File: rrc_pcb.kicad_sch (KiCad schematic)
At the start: 13 parts, among them J1 Voltage Regulator Input, J2 Conn_01x03_Male, U1 ADXL357Z, U2 Teensy3.6-teensy, U3 BN220-GPS, U4 MS5611, U5 logo

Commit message: updated .sch
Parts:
- removed RF11: RFD900+-RF_Module, rfd900+:RFD900+, symbol parts:RFD900+-RF_Module
- removed U1: ADXL357Z, adxl357z:ADXL357, symbol parts:ADXL357Z
- added U1: iridium9602, symbol parts:iridium9602
- added U6: ICM-20948, QFN40P300X300X105-24N, symbol parts:ICM-20948
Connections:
- net +5V: now also U1.1 (5V)
- net GND: now also U1.4 (GND)
- net T_GND: now also U6.18 (GND), U6.19 (RESV_19), U6.20 (RESV_20)
- net T_VCC: now also U6.13 (VDD), U6.8 (VDDIO)
- net RX2: now reaches U2.11 (9_PWM_RX2_CS0)
- net RX2: now also U1.3 (TX)
- net TX2: now reaches U2.12 (10_PWM_TX2_CS0)
- net TX2: now also U1.2 (RX)
- net at U2.45 (18_A4_SDA0_TOUCH): no longer R2.1
- net at U2.46 (19_A5_SCL0_TOUCH): no longer R1.1
- net at U2.~ (GND): now also R2.1, U6.24 (SDA/SDI)
- new net: R1.1, U2.~ (GND), U6.23 (SCL/SCLK)
- new net: U6.1 (NC), U6.14 (NC), U6.15 (NC), U6.16 (NC), U6.17 (NC), U6.2 (NC), U6.3 (NC), U6.4 (NC), U6.5 (NC), U6.6 (NC)
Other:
- moved on the sheet: J1, J2, R1, R2

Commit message: update 2
updated .sch added teensy4.1 , and updated footprints. Still in debugging stage
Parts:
- removed U2: Teensy3.6-teensy, teensy:Teensy35_36, symbol parts:Teensy3.6-teensy
- added U2: DEV-16771, teensy:Teensy41, symbol parts:DEV-16771
- U1: footprint (none) -> Connector_PinHeader_2.54mm:PinHeader_1x04_P2.54mm_Horizontal
- U4: renamed from U6; footprint QFN40P300X300X105-24N -> Connector_PinHeader_2.54mm:PinHeader_2x10_P2.54mm_Vertical
- renumbered U4 to U5, U5 to U6
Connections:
- net +5V: now also U2.VIN; no longer U1.1 (5V)
- net GND: now also U2.GND1 (GND), U2.GND2 (GND), U2.GND3 (GND), U2.GND4 (GND), U2.GND5 (GND)
- net RX2: now also U2.7 (RX2)
- net TX2: now also U2.8 (TX2)
- net T_GND: now also U2.USB_GND1 (USB_GND), U2.USB_GND2 (USB_GND)
- net T_VCC: now also U1.1 (5V), U2.5V
- net RX1: now reaches U3.3 (TX)
- net RX1: now also U2.0 (RX1)
- net at J2.2 (Pin_2): now also U2.23 (A9)
- net at BZ1.1 (-): now also U2.41 (A17)
- net TX1: now reaches U3.2 (RX)
- net TX1: now also U2.1 (TX1)
- net SCL1: now reaches R3.1, U5.3 (SCL)
- net SCL1: now also U2.16 (A2)
- net SDA1: now reaches R4.1, U5.4 (SDA)
- net SDA1: now also U2.17 (A3)
- net at R1.1, U4.23 (SCL/SCLK): now also U2.19 (A5)
- net at R2.1, U4.24 (SDA/SDI): now also U2.18 (A4)
- new net: U2.3.3V_1 (3.3V), U2.3.3V_2 (3.3V), U2.3.3V_3 (3.3V)
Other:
- moved on the sheet: BZ1, J1, J2, R1, R2, R3, R4, U1, U3, U4, U5, U6

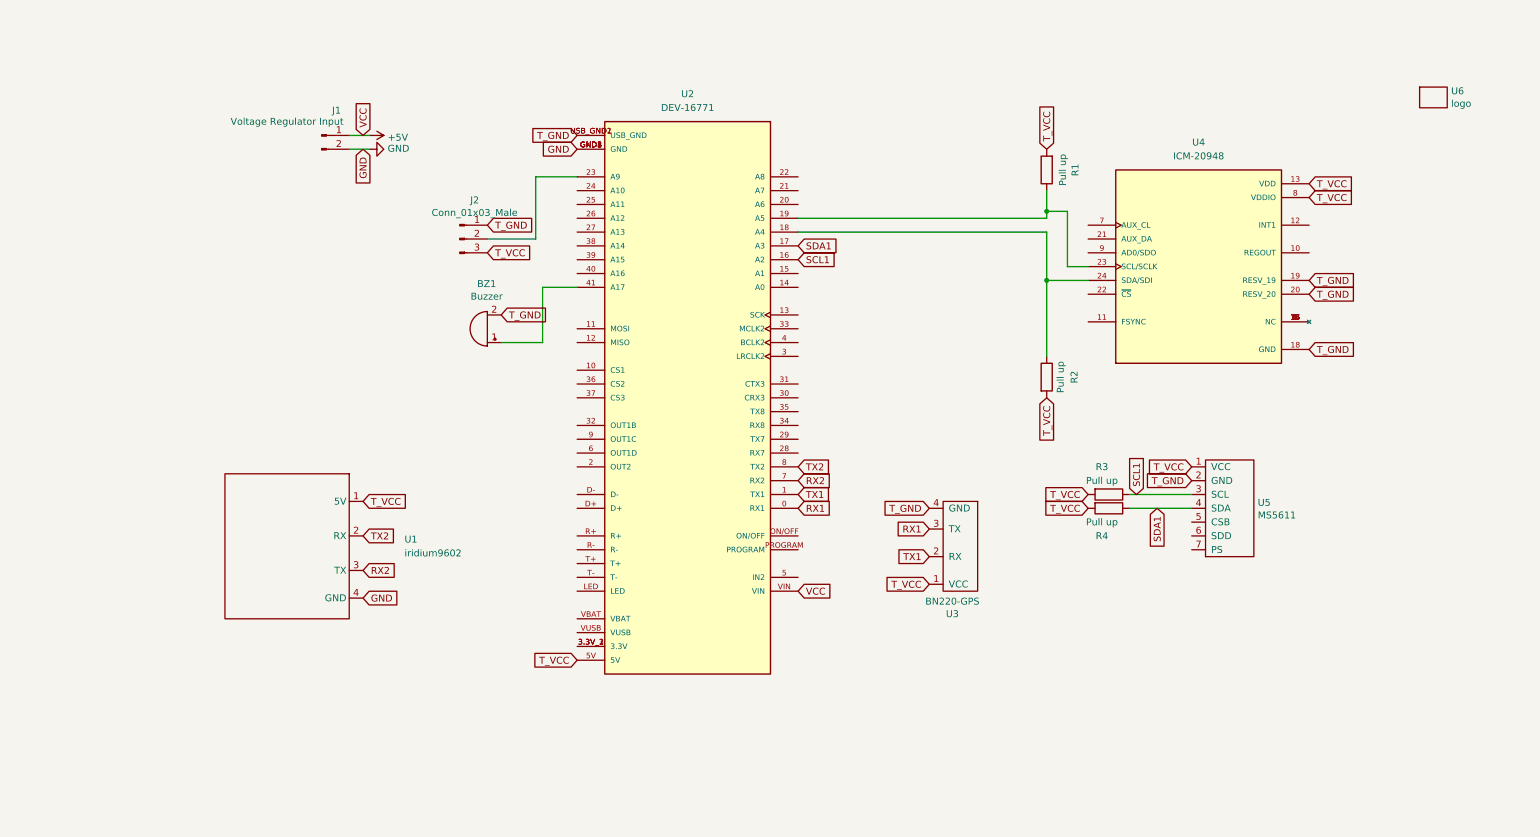
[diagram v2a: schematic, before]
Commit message: updated pcb footprints
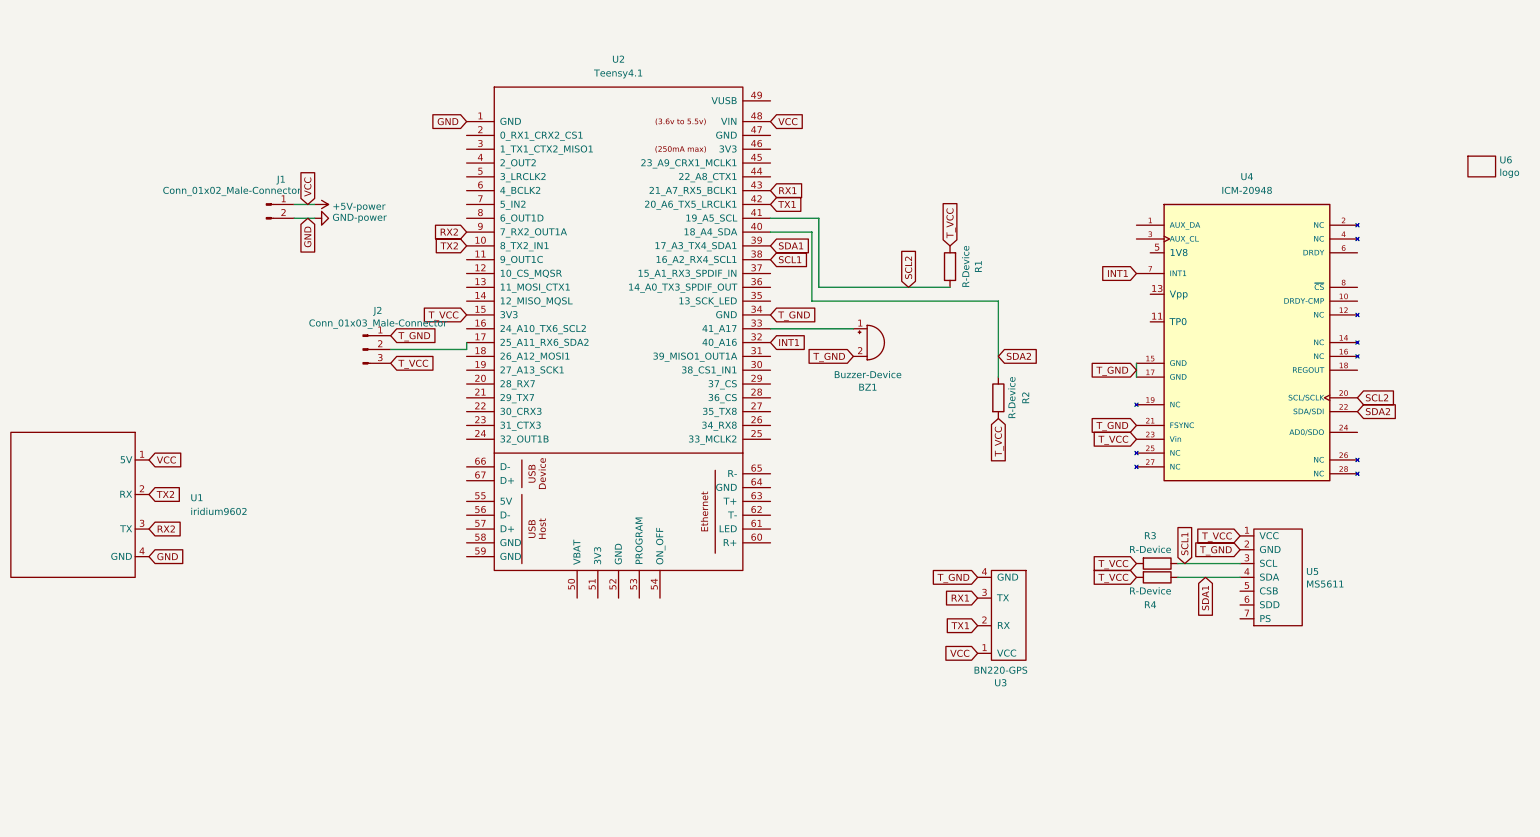
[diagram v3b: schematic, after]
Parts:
- removed U2: DEV-16771, teensy:Teensy41, symbol parts:DEV-16771
- removed U4: ICM-20948, Connector_PinHeader_2.54mm:PinHeader_2x10_P2.54mm_Vertical, symbol parts:ICM-20948
- added U2: Teensy4.1, teensy:Teensy41, symbol teensy:Teensy4.1
- added U4: ICM-20948, Connector_PinHeader_2.54mm:PinHeader_2x14_P2.54mm_Vertical, symbol parts:ICM-20948
- BZ1: value Buzzer -> Buzzer-Device
- J1: value Voltage Regulator Input -> Conn_01x02_Male-Connector
- J2: value Conn_01x03_Male -> Conn_01x03_Male-Connector
- R1, R2, R3, R4: value Pull up -> R-Device
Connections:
- net +5V: now also U1.1 (5V), U3.1 (VCC), U2.48 (VIN)
- net GND: now also U2.1 (GND)
- net RX1: now also U2.43 (21_A7_RX5_BCLK1)
- net RX2: now also U2.9 (7_RX2_OUT1A)
- net SCL1: now also U2.38 (16_A2_RX4_SCL1)
- net SDA1: now also U2.39 (17_A3_TX4_SDA1)
- net TX1: now also U2.42 (20_A6_TX5_LRCLK1)
- net TX2: now also U2.10 (8_TX2_IN1)
- net T_GND: now also U2.34 (GND), U4.15 (GND), U4.17 (GND), U4.21 (FSYNC)
- net T_VCC: now also U2.15 (3V3), U4.23 (Vin); no longer U1.1 (5V), U3.1 (VCC)
- net SCL2: now reaches R1.1
- net SCL2: now also U2.41 (19_A5_SCL), U4.20 (SCL/SCLK)
- net SDA2: now reaches R2.1
- net SDA2: now also U2.40 (18_A4_SDA), U4.22 (SDA/SDI)
- net at BZ1.1 (-): now also U2.33 (41_A17)
- net at J2.2 (Pin_2): now also U2.17 (25_A11_RX6_SDA2)
- new net INT1: U2.32 (40_A16), U4.7 (INT1)
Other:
- moved on the sheet: BZ1, J1, J2, R1, R2, R3, R4, U1, U3, U5, U6

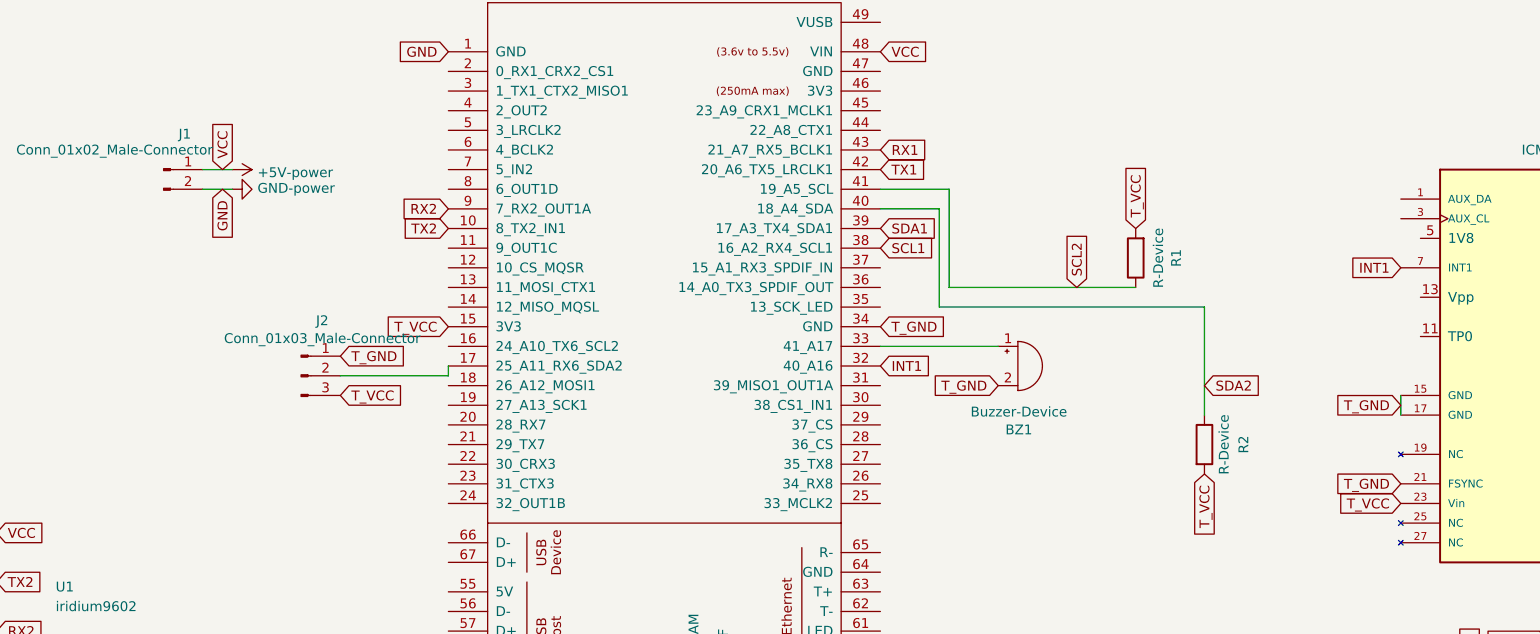
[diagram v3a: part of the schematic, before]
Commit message: optimized and finalized pcb
reduced sizing and fixed traces.
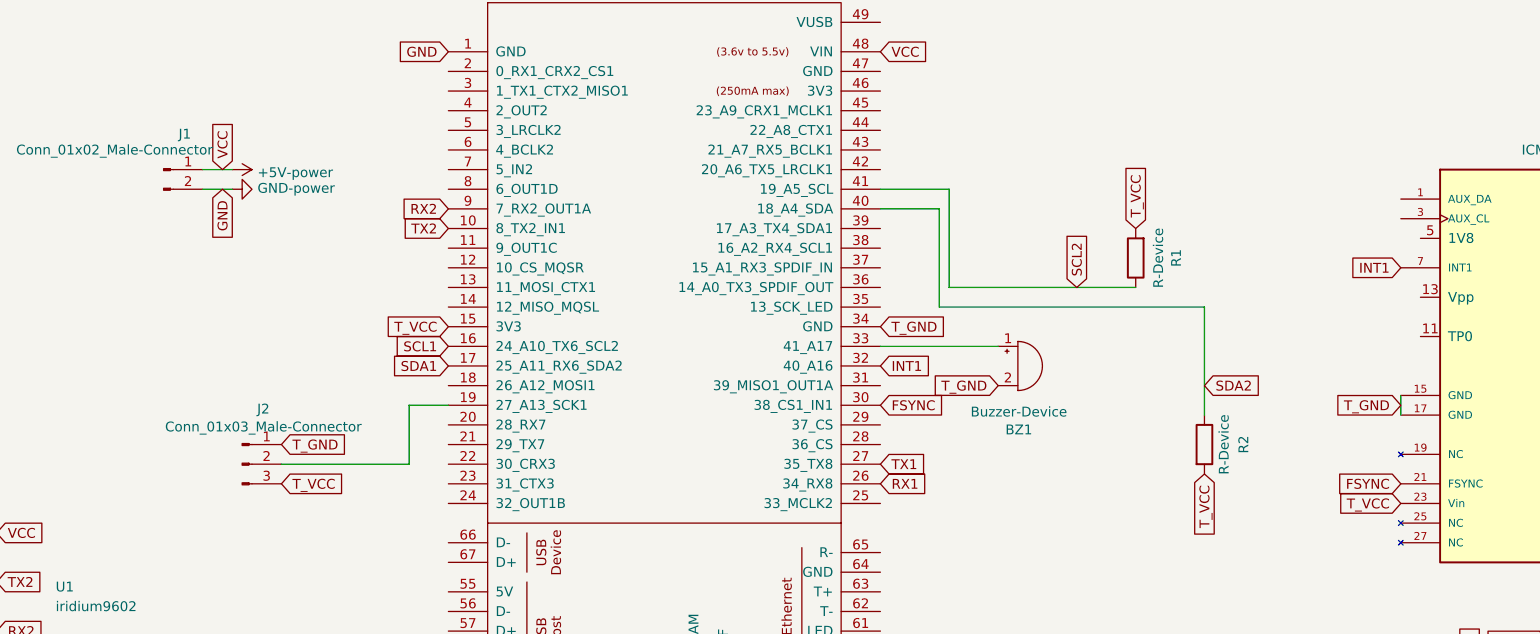
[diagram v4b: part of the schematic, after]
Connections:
- net RX1: now also U2.26 (34_RX8); no longer U2.43 (21_A7_RX5_BCLK1)
- net SCL1: now also U2.16 (24_A10_TX6_SCL2); no longer U2.38 (16_A2_RX4_SCL1)
- net SDA1: now also U2.17 (25_A11_RX6_SDA2); no longer U2.39 (17_A3_TX4_SDA1)
- net TX1: now also U2.27 (35_TX8); no longer U2.42 (20_A6_TX5_LRCLK1)
- net T_GND: no longer U4.21 (FSYNC)
- net at J2.2 (Pin_2): now also U2.19 (27_A13_SCK1); no longer U2.17 (25_A11_RX6_SDA2)
- net FSYNC: now reaches U2.30 (38_CS1_IN1)
- net FSYNC: now also U4.21 (FSYNC)
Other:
- moved on the sheet: J2
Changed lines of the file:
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@@
-    (stroke (width 0) (type default) (color 0 0 0 0))
-  )
-  (wire (pts (xy 85.09 63.5) (xy 99.06 63.5))
     (stroke (width 0) (type default) (color 0 0 0 0))
   )
@@
     (stroke (width 0) (type default) (color 0 0 0 0))
   )
+  (wire (pts (xy 77.47 74.93) (xy 93.98 74.93))
+    (stroke (width 0) (type default) (color 0 0 0 0))
+  )
   (wire (pts (xy 163.83 52.07) (xy 187.96 52.07))
     (stroke (width 0) (type default) (color 0 0 0 0))
@@
     (stroke (width 0) (type default) (color 0 0 0 0))
   )
+  (wire (pts (xy 93.98 67.31) (xy 99.06 67.31))
+    (stroke (width 0) (type default) (color 0 0 0 0))
+  )
+  (wire (pts (xy 93.98 74.93) (xy 93.98 67.31))
+    (stroke (width 0) (type default) (color 0 0 0 0))
+  )
   (wire (pts (xy 163.83 52.07) (xy 163.83 39.37))
     (stroke (width 0) (type default) (color 0 0 0 0))
@@
     (stroke (width 0) (type default) (color 0 0 0 0))
   )
-  (wire (pts (xy 99.06 63.5) (xy 99.06 62.23))
-    (stroke (width 0) (type default) (color 0 0 0 0))
-  )
   (wire (pts (xy 162.56 54.61) (xy 162.56 41.91))
     (stroke (width 0) (type default) (color 0 0 0 0))
   )
+  (global_label "FSYNC" (shape input) (at 222.25 77.47 180) (fields_autoplaced)
+    (effects (font (size 1.27 1.27)) (justify right))
+    (property "Intersheet References" "${INTERSHEET_REFS}" (id 0) (at 213.9387 77.3906 0)
+      (effects (font (size 1.27 1.27)) (justify right) hide)
+    )
+  )
   (global_label "T_GND" (shape input) (at 222.25 67.31 180) (fields_autoplaced)
     (effects (font (size 1.27 1.27)) (justify right))
@@
     )
   )
-  (global_label "TX1" (shape input) (at 154.94 36.83 0) (fields_autoplaced)
-    (effects (font (size 1.27 1.27)) (justify left))
-    (property "Intersheet References" "${INTERSHEET_REFS}" (id 0) (at 160.6509 36.7506 0)
-      (effects (font (size 1.27 1.27)) (justify left) hide)
-    )
-  )
-  (global_label "SDA1" (shape input) (at 154.94 44.45 0) (fields_autoplaced)
-    (effects (font (size 1.27 1.27)) (justify left))
-    (property "Intersheet References" "${INTERSHEET_REFS}" (id 0) (at 162.0418 44.3706 0)
-      (effects (font (size 1.27 1.27)) (justify left) hide)
-    )
-  )
-  (global_label "T_GND" (shape input) (at 85.09 60.96 0) (fields_autoplaced)
-    (effects (font (size 1.27 1.27)) (justify left))
-    (property "Intersheet References" "${INTERSHEET_REFS}" (id 0) (at 20.32 -59.69 0)
+  (global_label "T_GND" (shape input) (at 77.47 72.39 0) (fields_autoplaced)
+    (effects (font (size 1.27 1.27)) (justify left))
+    (property "Intersheet References" "${INTERSHEET_REFS}" (id 0) (at 12.7 -48.26 0)
       (effects (font (size 1.27 1.27)) hide)
     )
@@
     )
   )
-  (global_label "T_VCC" (shape input) (at 85.09 66.04 0) (fields_autoplaced)
-    (effects (font (size 1.27 1.27)) (justify left))
-    (property "Intersheet References" "${INTERSHEET_REFS}" (id 0) (at 20.32 -59.69 0)
-      (effects (font (size 1.27 1.27)) hide)
-    )
-  )
-  (global_label "RX1" (shape input) (at 154.94 34.29 0) (fields_autoplaced)
-    (effects (font (size 1.27 1.27)) (justify left))
-    (property "Intersheet References" "${INTERSHEET_REFS}" (id 0) (at 160.9532 34.2106 0)
+  (global_label "RX1" (shape input) (at 154.94 77.47 0) (fields_autoplaced)
+    (effects (font (size 1.27 1.27)) (justify left))
+    (property "Intersheet References" "${INTERSHEET_REFS}" (id 0) (at 160.9532 77.3906 0)
+      (effects (font (size 1.27 1.27)) (justify left) hide)
+    )
+  )
+  (global_label "T_VCC" (shape input) (at 77.47 77.47 0) (fields_autoplaced)
+    (effects (font (size 1.27 1.27)) (justify left))
+    (property "Intersheet References" "${INTERSHEET_REFS}" (id 0) (at 12.7 -48.26 0)
+      (effects (font (size 1.27 1.27)) hide)
+    )
+  )
+  (global_label "FSYNC" (shape input) (at 154.94 67.31 0) (fields_autoplaced)
+    (effects (font (size 1.27 1.27)) (justify left))
+    (property "Intersheet References" "${INTERSHEET_REFS}" (id 0) (at 163.2513 67.2306 0)
       (effects (font (size 1.27 1.27)) (justify left) hide)
     )
@@
     )
   )
+  (global_label "SCL1" (shape input) (at 99.06 59.69 180) (fields_autoplaced)
+    (effects (font (size 1.27 1.27)) (justify right))
+    (property "Intersheet References" "${INTERSHEET_REFS}" (id 0) (at 92.0187 59.6106 0)
+      (effects (font (size 1.27 1.27)) (justify right) hide)
+    )
+  )
   (global_label "T_VCC" (shape input) (at 222.25 80.01 180) (fields_autoplaced)
     (effects (font (size 1.27 1.27)) (justify right))
@@
     )
   )
+  (global_label "SDA1" (shape input) (at 99.06 62.23 180) (fields_autoplaced)
+    (effects (font (size 1.27 1.27)) (justify right))
+    (property "Intersheet References" "${INTERSHEET_REFS}" (id 0) (at 91.9582 62.3094 0)
+      (effects (font (size 1.27 1.27)) (justify right) hide)
+    )
+  )
   (global_label "INT1" (shape input) (at 222.25 49.53 180) (fields_autoplaced)
     (effects (font (size 1.27 1.27)) (justify right))
@@
     )
   )
-  (global_label "T_GND" (shape input) (at 222.25 77.47 180) (fields_autoplaced)
-    (effects (font (size 1.27 1.27)) (justify right))
-    (property "Intersheet References" "${INTERSHEET_REFS}" (id 0) (at 361.95 -162.56 0)
-      (effects (font (size 1.27 1.27)) hide)
-    )
-  )
   (global_label "T_GND" (shape input) (at 241.3 100.33 180) (fields_autoplaced)
     (effects (font (size 1.27 1.27)) (justify right))
@@
     )
   )
-  (global_label "SCL1" (shape input) (at 154.94 46.99 0) (fields_autoplaced)
-    (effects (font (size 1.27 1.27)) (justify left))
-    (property "Intersheet References" "${INTERSHEET_REFS}" (id 0) (at 161.9813 47.0694 0)
-      (effects (font (size 1.27 1.27)) (justify left) hide)
-    )
-  )
   (global_label "T_GND" (shape input) (at 154.94 57.15 0) (fields_autoplaced)
     (effects (font (size 1.27 1.27)) (justify left))
@@
     (effects (font (size 1.27 1.27)) (justify left))
     (property "Intersheet References" "${INTERSHEET_REFS}" (id 0) (at 269.9313 72.3106 0)
+      (effects (font (size 1.27 1.27)) (justify left) hide)
+    )
+  )
+  (global_label "TX1" (shape input) (at 154.94 74.93 0) (fields_autoplaced)
+    (effects (font (size 1.27 1.27)) (justify left))
+    (property "Intersheet References" "${INTERSHEET_REFS}" (id 0) (at 160.6509 74.8506 0)
       (effects (font (size 1.27 1.27)) (justify left) hide)
     )
@@
     )
   )
-  (symbol (lib_id "rrc_pcb-rescue:Conn_01x03_Male-Connector") (at 80.01 63.5 0) (unit 1)
-    (in_bom yes) (on_board yes)
-    (property "Reference" "J2" (id 0) (at 82.7532 56.3626 0))
-    (property "Value" "Conn_01x03_Male-Connector" (id 1) (at 82.7532 58.674 0))
-    (property "Footprint" "Connector_PinHeader_2.54mm:PinHeader_1x03_P2.54mm_Vertical" (id 2) (at 80.01 63.5 0)
-      (effects (font (size 1.27 1.27)) hide)
-    )
-    (property "Datasheet" "~" (id 3) (at 80.01 63.5 0)
-      (effects (font (size 1.27 1.27)) hide)
-    )
+  (symbol (lib_id "rrc_pcb-rescue:Conn_01x03_Male-Connector") (at 72.39 74.93 0) (unit 1)
+    (in_bom yes) (on_board yes)
+    (property "Reference" "J2" (id 0) (at 75.1332 67.7926 0))
+    (property "Value" "Conn_01x03_Male-Connector" (id 1) (at 75.1332 70.104 0))
+    (property "Footprint" "Connector_PinHeader_2.54mm:PinHeader_1x03_P2.54mm_Vertical" (id 2) (at 72.39 74.93 0)
+      (effects (font (size 1.27 1.27)) hide)
+    )
+    (property "Datasheet" "~" (id 3) (at 72.39 74.93 0)
+      (effects (font (size 1.27 1.27)) hide)
+    )
